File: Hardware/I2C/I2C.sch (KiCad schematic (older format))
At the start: 5 parts, among them P1 DIL16, P2 CONN_01X04

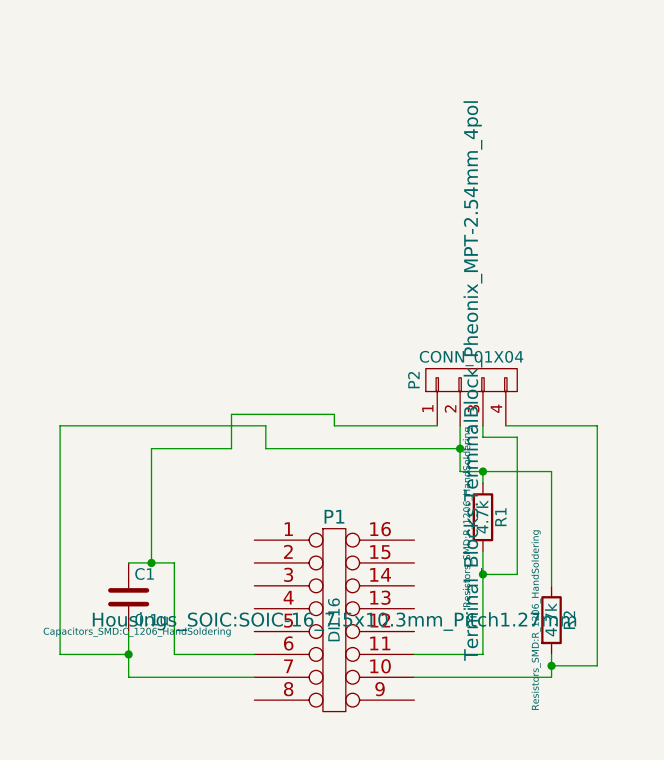
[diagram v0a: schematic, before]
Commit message: updated I2C design, added various exports used in testing with cnc machine
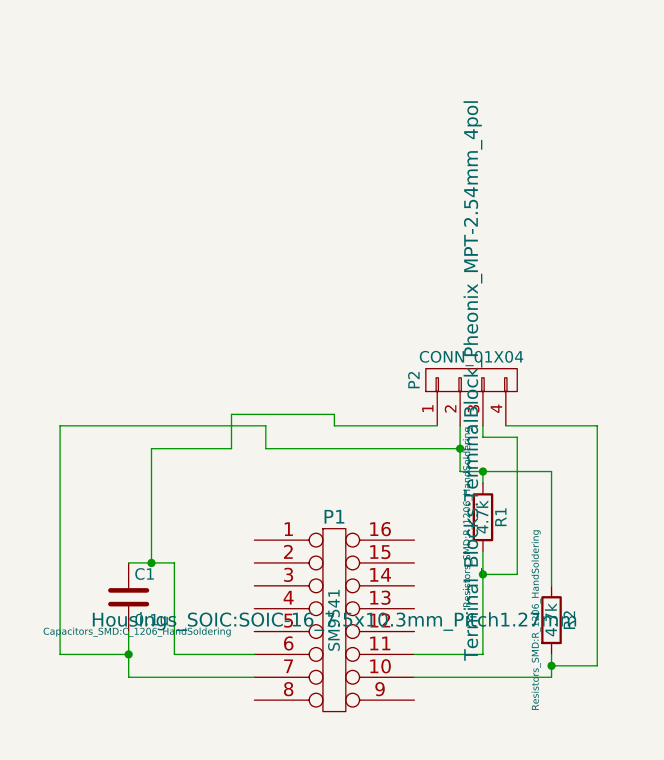
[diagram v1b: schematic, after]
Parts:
- P1: value DIL16 -> SM9541
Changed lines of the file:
@@
 P 3850 3100
 F 0 "P1" H 3850 3550 60  0000 C CNN
-F 1 "DIL16" V 3850 3100 50  0000 C CNN
+F 1 "SM9541" V 3850 3100 50  0000 C CNN
 F 2 "Housings_SOIC:SOIC-16_7.5x10.3mm_Pitch1.27mm" H 3850 3100 60  0000 C CNN
 F 3 "" H 3850 3100 60  0000 C CNN
